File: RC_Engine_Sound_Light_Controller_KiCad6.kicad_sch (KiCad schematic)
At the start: 35 parts, among them J1 RX, J10 RGB, J11 32, J12 CH1, J13 CH2, J14 CH3, J15 ESC, J16 CH4, J2 HeadL, J3 TailL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

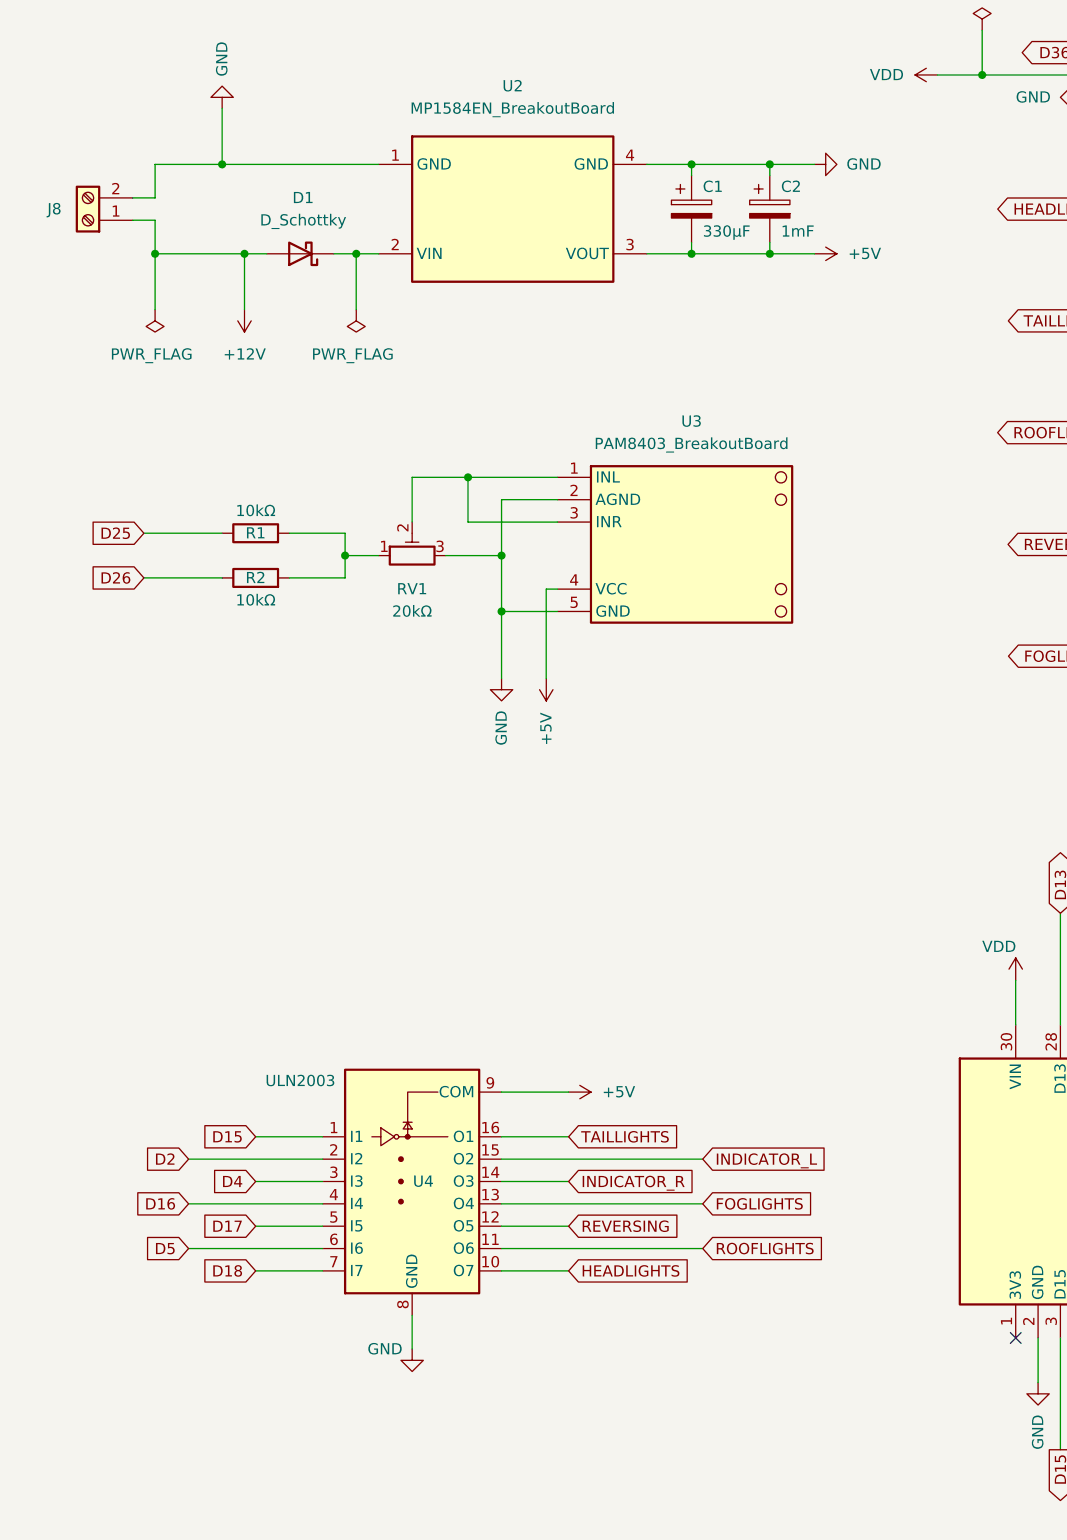
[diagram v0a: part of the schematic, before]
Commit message: Added RZ7886 to schematic
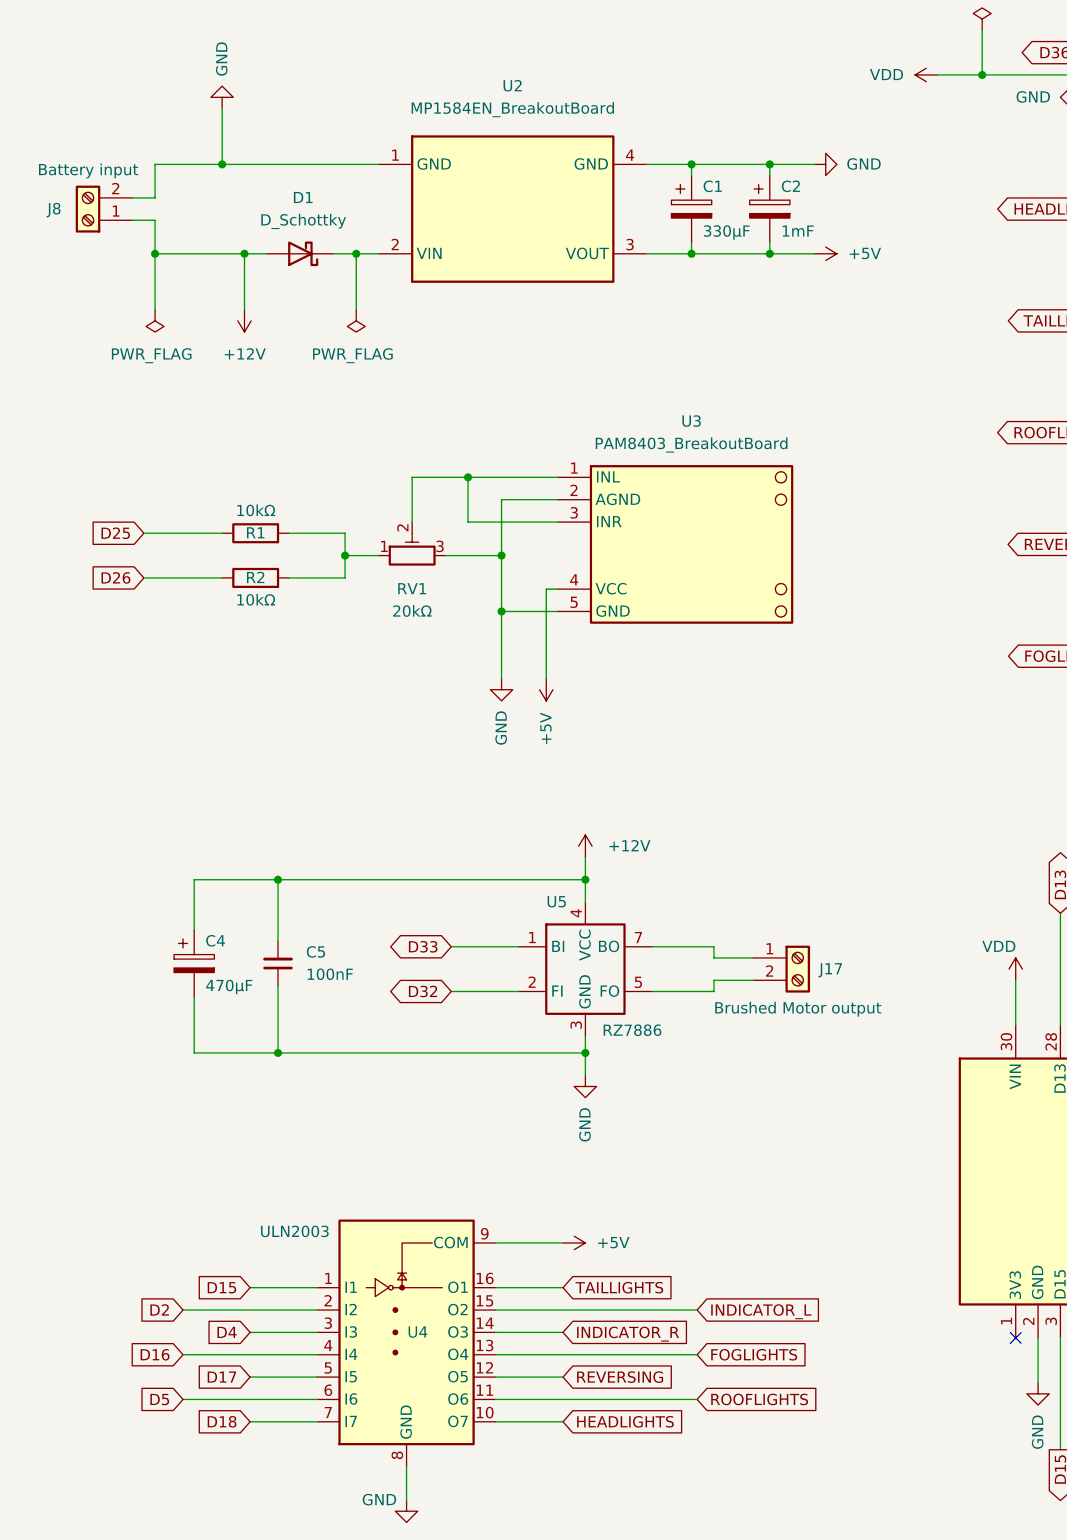
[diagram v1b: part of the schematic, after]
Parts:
- added C4: 470µF, Capacitor_THT:CP_Radial_D10.0mm_P2.50mm_P5.00mm, symbol Device:C_Polarized
- added C5: 100nF, Capacitor_SMD:C_1206_3216Metric_Pad1.33x1.80mm_HandSolder, symbol Device:C_Small
- added J17: Brushed Motor output, cf:InputPowerSolderPads, symbol Connector:Screw_Terminal_01x02
- added U5: RZ7886, cf:RZ7886_DIP8, symbol cf:RZ7886
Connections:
- net +12V: now also C4.1, C5.2, U5.4 (VCC)
- net D32: now also U5.2 (FI)
- net D33: now also U5.1 (BI)
- net GND: now also C4.2, C5.1, U5.3 (GND)
- new net: J17.2 (Pin_2), U5.5 (FO), U5.6 (FO)
- new net: J17.1 (Pin_1), U5.7 (BO), U5.8 (BO)
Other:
- moved on the sheet: U4

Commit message: All but data lines routed
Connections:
- net CH2: now reaches J13.1 (Pin_1), R8.2
- net CH1: now reaches J12.1 (Pin_1), R9.2
- net +10V: now reaches D1.1 (K), U2.2 (VIN), U2.6 (VIN)
- net ESC: now reaches J15.1 (Pin_1), R5.2
- net MOTOR_FO: now reaches J17.2 (Pin_2), U5.5 (FO), U5.6 (FO)
- net MOTOR_BO: now reaches J17.1 (Pin_1), U5.7 (BO), U5.8 (BO)
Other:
- moved on the sheet: D1

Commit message: Pins 32 and 33 connected to driver IC.
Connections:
- net RX: now reaches J1.1 (Pin_1), R3.2
- net AUDIO_JOINT: now reaches R1.2, R2.2, RV1.1
- net PIN_32: now reaches J11.1 (Pin_1), R4.2
- net RGB: now reaches J10.1 (Pin_1), R10.2
- net CH3: now reaches J14.1 (Pin_1), R7.2
- net AUDIO_IN: now reaches RV1.2, U3.1 (INL), U3.3 (INR)
- net CH4: now reaches J16.1 (Pin_1), R6.2
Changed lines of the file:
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@@
     (stroke (width 0) (type default) (color 0 0 0 0))
+  )
+  (label "CH3" (at 266.7 67.31 90)
+    (effects (font (size 1.27 1.27)) (justify left bottom))
+  )
+  (label "RX" (at 147.32 22.86 90)
+    (effects (font (size 1.27 1.27)) (justify left bottom))
   )
   (label "ESC" (at 266.7 22.86 90)
@@
     (effects (font (size 1.27 1.27)) (justify right bottom))
   )
+  (label "AUDIO_IN" (at 59.055 71.12 90)
+    (effects (font (size 1.27 1.27)) (justify left bottom))
+  )
   (label "CH1" (at 266.7 38.1 90)
+    (effects (font (size 1.27 1.27)) (justify left bottom))
+  )
+  (label "CH4" (at 266.7 82.55 90)
     (effects (font (size 1.27 1.27)) (justify left bottom))
   )
@@
     (effects (font (size 1.27 1.27)) (justify left bottom))
   )
+  (label "RGB" (at 207.01 36.83 90)
+    (effects (font (size 1.27 1.27)) (justify left bottom))
+  )
+  (label "AUDIO_JOINT" (at 51.435 80.01 270)
+    (effects (font (size 1.27 1.27)) (justify right bottom))
+  )
   (label "MOTOR_BO" (at 90.17 124.46 90)
     (effects (font (size 1.27 1.27)) (justify left bottom))
   )
+  (label "PIN_32" (at 207.01 22.86 90)
+    (effects (font (size 1.27 1.27)) (justify left bottom))
+  )

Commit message: Added seconds tantal cap.
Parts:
- added C6: 330µF, Capacitor_Tantalum_SMD:CP_EIA-7343-30_AVX-N_Pad2.25x2.55mm_HandSolder, symbol Device:C_Polarized
- added D2: USB Supply Protection, Diode_SMD:D_SMA-SMB_Universal_Handsoldering, symbol Device:D_Schottky
- D1: value D_Schottky -> Polarity Protection
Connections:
- net +12V: now also C6.1
- net GND: now also C6.2
- net VDD: now also D2.2 (A); no longer U1.30 (VIN)
- new net: D2.1 (K), U1.30 (VIN)
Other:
- moved on the sheet: C4, C5

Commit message: Removed ESC and Pin 32 headers.
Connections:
- net VDD is gone; now on net +5V: D2.2 (A), J1.2 (Pin_2), J11.2 (Pin_2), J12.2 (Pin_2), J13.2 (Pin_2), J14.2 (Pin_2), J15.2 (Pin_2), J16.2 (Pin_2)
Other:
- note added: "Hidden in the current PCB design!"

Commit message: Added voltage divider for battery voltage measurement. Renamed power nets.
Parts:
- added C7: 100nF, Capacitor_SMD:C_1206_3216Metric_Pad1.33x1.80mm_HandSolder, symbol Device:C
- added R11: 570kΩ, Resistor_SMD:R_0805_2012Metric_Pad1.20x1.40mm_HandSolder, symbol Device:R
- added R12: 330kΩ, Resistor_SMD:R_0805_2012Metric_Pad1.20x1.40mm_HandSolder, symbol Device:R
- renumbered C4 to C1, C5 to C3, C3 to C4, C1 to C5
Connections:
- net D39: now reaches U1.18 (D39)
- net D39: now also C7.1, R11.2, R12.1
- net +10V: no longer names the net of D1.1 (K), U2.2 (VIN), U2.6 (VIN)
- net +12V renamed +BATT
- net +BATT: now also R11.1
- net +5V renamed VCC
- net GND renamed -BATT
- net -BATT: now also C7.2, R12.2
- no-connect marks 9 -> 8
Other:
- note added: "Auto upload fix"
- note added: "Battery voltage measurement"

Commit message: Some minor changes.
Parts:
- D1, D2: footprint Diode_SMD:D_SMA-SMB_Universal_Handsoldering -> Diode_SMD:D_SMA_Handsoldering
- R11: value 570kΩ -> 100kΩ
- R12: value 330kΩ -> 22kΩ
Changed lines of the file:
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@@
       (effects (font (size 1.27 1.27)) (justify left))
     )
-    (property "Value" "330kΩ" (id 1) (at 232.41 139.6999 0)
+    (property "Value" "22kΩ" (id 1) (at 232.41 139.6999 0)
       (effects (font (size 1.27 1.27)) (justify left))
     )
@@
       (effects (font (size 1.27 1.27)) (justify right))
     )
-    (property "Footprint" "Diode_SMD:D_SMA-SMB_Universal_Handsoldering" (id 2) (at 124.46 124.46 0)
+    (property "Footprint" "Diode_SMD:D_SMA_Handsoldering" (id 2) (at 124.46 124.46 0)
       (effects (font (size 1.27 1.27)) hide)
     )
@@
       (effects (font (size 1.27 1.27)) (justify left))
     )
-    (property "Value" "570kΩ" (id 1) (at 232.41 126.9999 0)
+    (property "Value" "100kΩ" (id 1) (at 232.41 126.9999 0)
       (effects (font (size 1.27 1.27)) (justify left))
     )
@@
     (property "Reference" "D1" (id 0) (at 39.6875 39.37 0))
     (property "Value" "Polarity Protection" (id 1) (at 39.6875 41.91 0))
-    (property "Footprint" "Diode_SMD:D_SMA-SMB_Universal_Handsoldering" (id 2) (at 39.37 45.72 0)
+    (property "Footprint" "Diode_SMD:D_SMA_Handsoldering" (id 2) (at 39.37 45.72 0)
       (effects (font (size 1.27 1.27)) hide)
     )
@@
     )
     (path "/eca3bb7b-a37d-4395-81c5-81f63a2b25c0"
-      (reference "D1") (unit 1) (value "Polarity Protection") (footprint "Diode_SMD:D_SMA-SMB_Universal_Handsoldering")
+      (reference "D1") (unit 1) (value "Polarity Protection") (footprint "Diode_SMD:D_SMA_Handsoldering")
     )
     (path "/ba8a55b9-9a74-4560-a9f1-9a5c827e8a40"
-      (reference "D2") (unit 1) (value "USB Supply Protection") (footprint "Diode_SMD:D_SMA-SMB_Universal_Handsoldering")
+      (reference "D2") (unit 1) (value "USB Supply Protection") (footprint "Diode_SMD:D_SMA_Handsoldering")
     )
     (path "/03b5281b-f2b9-42ca-84a7-e7f14e3aaaa5"
@@
     )
     (path "/df4099de-e302-45a1-8aaa-fe41f5afb6c2"
-      (reference "R11") (unit 1) (value "570kΩ") (footprint "Resistor_SMD:R_0805_2012Metric_Pad1.20x1.40mm_HandSolder")
+      (reference "R11") (unit 1) (value "100kΩ") (footprint "Resistor_SMD:R_0805_2012Metric_Pad1.20x1.40mm_HandSolder")
     )
     (path "/5a2d737e-c57a-4078-acc1-bc5a7b277d46"
-      (reference "R12") (unit 1) (value "330kΩ") (footprint "Resistor_SMD:R_0805_2012Metric_Pad1.20x1.40mm_HandSolder")
+      (reference "R12") (unit 1) (value "22kΩ") (footprint "Resistor_SMD:R_0805_2012Metric_Pad1.20x1.40mm_HandSolder")
     )
     (path "/e083cc61-af2b-4d98-89a2-774b290b996d"
